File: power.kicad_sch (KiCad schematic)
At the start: 36 parts, among them J1 XT30PW-M, U1 ZXCT1107, U2 ST715M25R

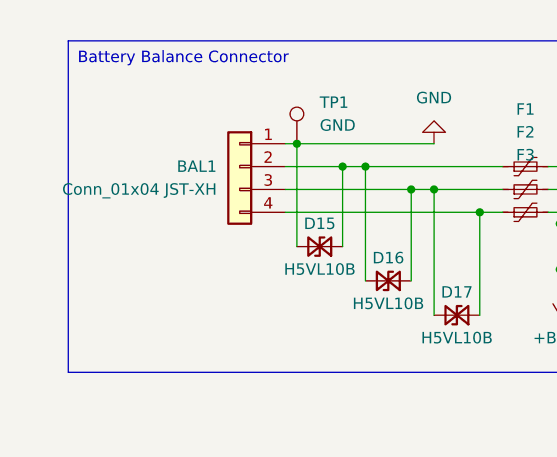
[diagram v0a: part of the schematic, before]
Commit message: Basic charging code, stupid power connector was reversed
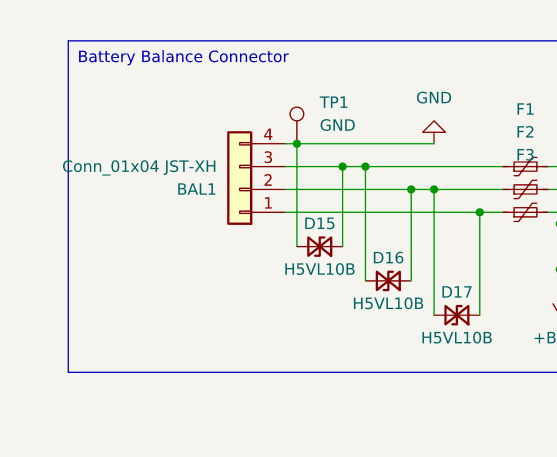
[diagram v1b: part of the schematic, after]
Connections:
- net GND: now also BAL1.4 (Pin_4); no longer BAL1.1 (Pin_1)
- net at D17.1 (A1), F3.1: now also BAL1.1 (Pin_1); no longer BAL1.4 (Pin_4)
- net at D15.1 (A1), D16.2 (A2), F1.1: now also BAL1.3 (Pin_3); no longer BAL1.2 (Pin_2)
- net at D16.1 (A1), D17.2 (A2), F2.1: now also BAL1.2 (Pin_2); no longer BAL1.3 (Pin_3)
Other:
- moved on the sheet: BAL1
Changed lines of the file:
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@@
 	(symbol
 		(lib_id "Connector_Generic:Conn_01x04")
-		(at 44.45 41.91 0)
-		(mirror y)
+		(at 44.45 44.45 180)
 		(unit 1)
 		(exclude_from_sim no)
@@
 		(dnp no)
 		(property "Reference" "BAL1"
-			(at 41.91 41.9099 0)
+			(at 41.91 44.4501 0)
 			(effects
 				(font
@@
 		)
 		(property "Value" "Conn_01x04 JST-XH"
-			(at 41.91 44.4499 0)
+			(at 41.91 41.9101 0)
 			(effects
 				(font
@@
 		)
 		(property "Footprint" "JakeLib:JST_XH_S4B-XH-A_1x04_P2.50mm_Horizontal_Tight"
-			(at 44.45 41.91 0)
+			(at 44.45 44.45 0)
 			(effects
 				(font
@@
 		)
 		(property "Datasheet" "~"
-			(at 44.45 41.91 0)
+			(at 44.45 44.45 0)
 			(effects
 				(font
@@
 		)
 		(property "Description" "Generic connector, single row, 01x04, script generated (kicad-library-utils/schlib/autogen/connector/)"
-			(at 44.45 41.91 0)
+			(at 44.45 44.45 0)
 			(effects
 				(font
@@
 		)
 		(property "LCSC_Code" "C157925"
-			(at 44.45 41.91 0)
+			(at 44.45 44.45 0)
 			(effects
 				(font

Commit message: Taking notes, doing some final adjustments to RC filter values
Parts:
- removed C6: .1u, Capacitor_SMD:C_0603_1608Metric, symbol Device:C
- removed D2: BAT54SW, Package_TO_SOT_SMD:SOT-323_SC-70, symbol Diode:BAT54SW
- removed R10, R11, R6, R7: 47.5k, Resistor_SMD:R_0402_1005Metric, symbol Device:R
- removed R8, R9: 220k, Resistor_SMD:R_0402_1005Metric, symbol Device:R
- added C17: .1u, Capacitor_SMD:C_0603_1608Metric, symbol Device:C
- added R31, R32: 150, Resistor_SMD:R_0402_1005Metric, symbol Device:R
- R4: value 220k -> 2k; footprint Resistor_SMD:R_0402_1005Metric -> Resistor_SMD:R_0603_1608Metric; LCSC_Code C851925 -> (none); Tolerance 0.5% -> (none)
- R5: value 220k -> 18k; footprint Resistor_SMD:R_0402_1005Metric -> Resistor_SMD:R_0603_1608Metric; LCSC_Code C851925 -> (none); Tolerance 0.5% -> (none)
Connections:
- net GND: now also R4.1, C17.1
- net SOLAR_CURRENT_ADC: now also C17.2, R32.2; no longer R1.1, U1.3 (OUT)
- net VSOLAR: now also R5.2
- net VSOLAR_ADC: now also R4.2, R5.1
- new net: R1.1, R31.1, U1.3 (OUT)
- new net: R31.2, R32.1
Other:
- note added: "25V*(2000/(20000))=2.5V 25V/20000ohms = 1.25mA current draw ~30mW power dissipation 1.8kohm Thevenin impedance"
- note added: "Measure current "before" the vsolar capacitor bank so you see the smoother average power draw"
- note added: "RC filter with TC ~5khz 16x attentuation @ 80khz pwm loop Only 300 ohm extra impedance for adc"
- note added: "Rsense = .1 ohm, @ 2 amps = 0.2V (Recommended for full range is 0.5V drop, but that's wasteful) Iout = 0.004 * Vsense so 3000 * .004*.2 = 2.4V @ 2 amps current"
- note added: "Solar input maxes: 50V capacitors 30V MOSFET Drain-Source Breakdown 30V TVS Diode"
- note added: "The ZXCT has a defined current that it outputs for a given voltage. This is fine if you never sample the signal. But I am seeing on the scope two spike with each PWM cycle. I think what's happening is that the ADC turns on, and there is all of a sudden a small 1000ohm path to ground while charging/discharging the ADC capacitor so probably to eliminate that you need an opamp"
- note removed: "Rsense = .1 ohm, @ 2 amps = 0.2V (Recommended for full range is 0.5V drop, but that's too much) Iout = 0.004 * Vsense so 3000 * .004*.2 = 2.4V @ 2 amps current"
- note removed: "Solar input maxes: 50V capacitors 30V MOSFET Drain-Source Breakdown 25V IRS2003 10V battery -> 20V charge pump, 2.5V gate-source = 17Volts"
- note removed: "Using || higher precision resistors to reduce absolute error on balancing Also, each divider uses the same range (even the 1S and 2S ones), so that you have consistency. 110k || 23.75k => 19.5k impedance 19.5k ohm * 0.1u cap = 2ms 12*(47.5/(47.5+220)) ~= 2.1V"
- moved on the sheet: C7, D1, D3, R1, TP3

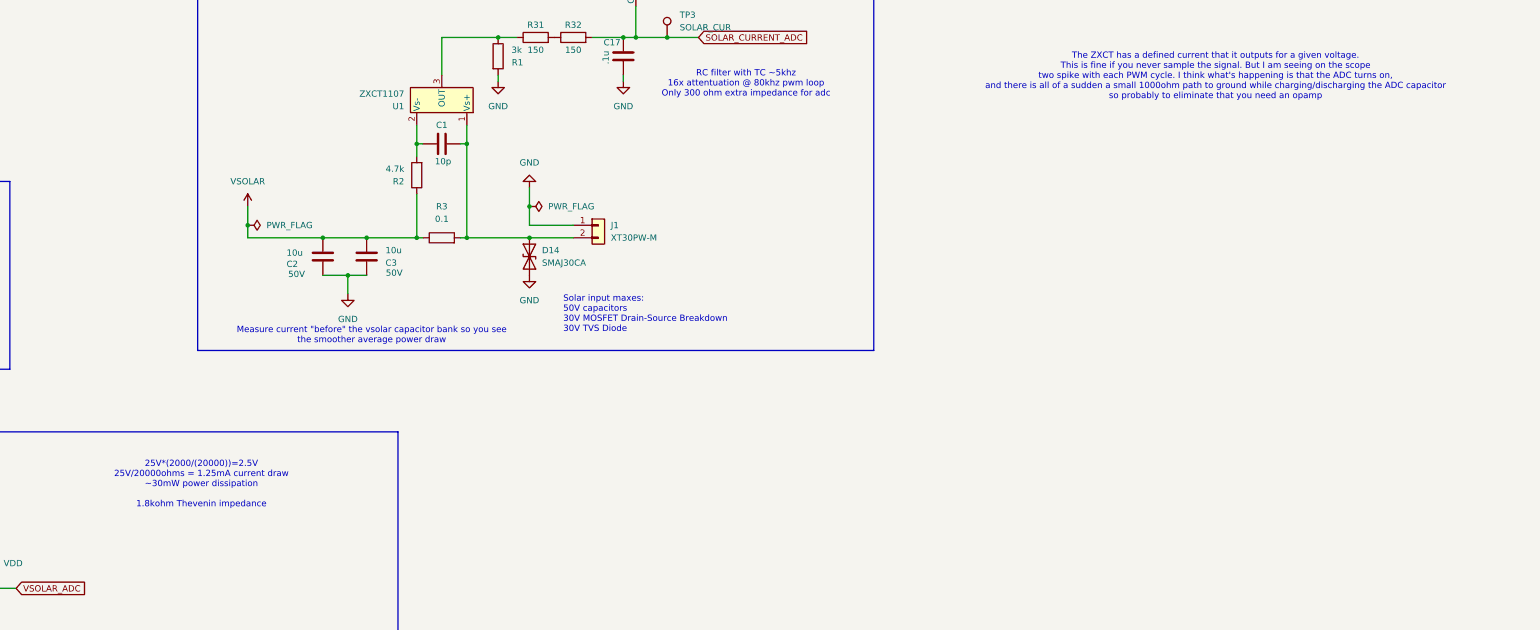
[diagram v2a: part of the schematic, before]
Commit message: L6388E mosfet drivers
Allow to enable/disable drivers
voltage dividers picked out
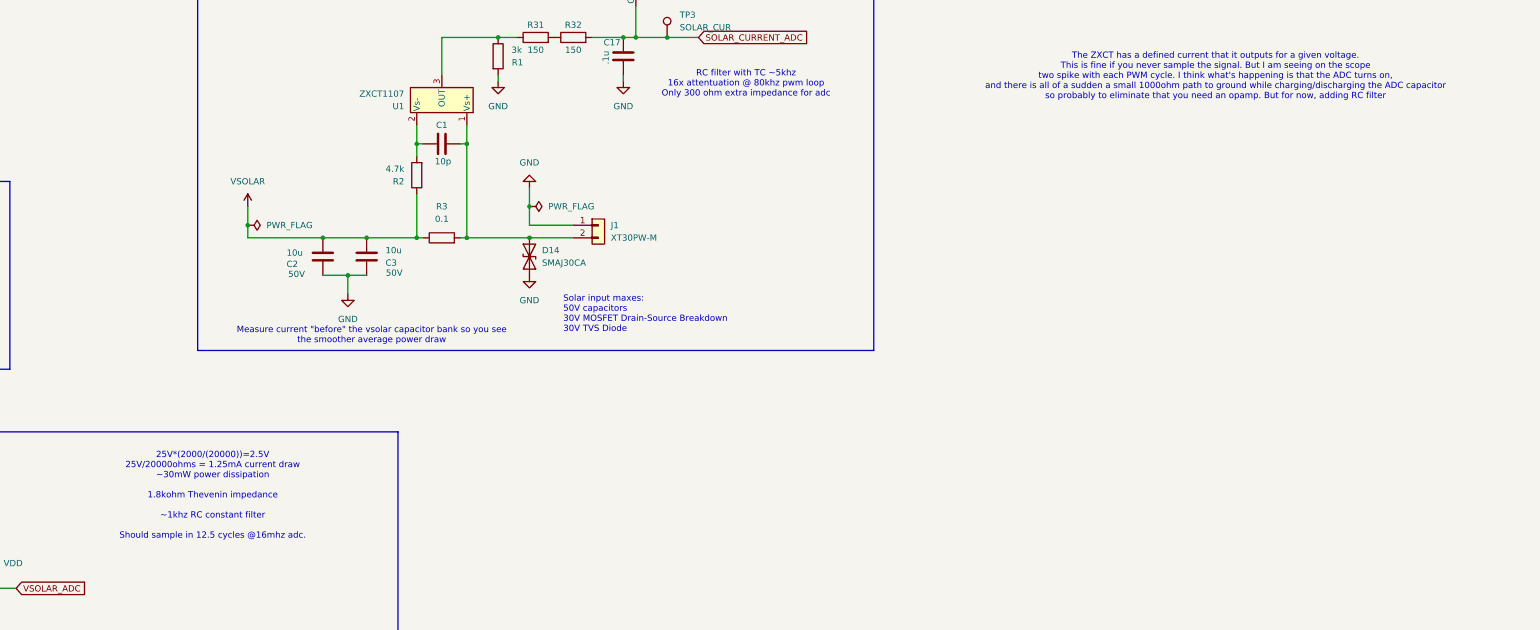
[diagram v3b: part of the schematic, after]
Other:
- note added: "25V*(2000/(20000))=2.5V 25V/20000ohms = 1.25mA current draw ~30mW power dissipation 1.8kohm Thevenin impedance ~1khz RC constant filter Should sample in 12.5 cycles @16mhz adc."
- note added: "The ZXCT has a defined current that it outputs for a given voltage. This is fine if you never sample the signal. But I am seeing on the scope two spike with each PWM cycle. I think what's happening is that the ADC turns on, and there is all of a sudden a small 1000ohm path to ground while charging/discharging the ADC capacitor so probably to eliminate that you need an opamp. But for now, adding R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"
- note removed: "25V*(2000/(20000))=2.5V 25V/20000ohms = 1.25mA current draw ~30mW power dissipation 1.8kohm Thevenin impedance"
- note removed: "The ZXCT has a defined current that it outputs for a given voltage. This is fine if you never sample the signal. But I am seeing on the scope two spike with each PWM cycle. I think what's happening is that the ADC turns on, and there is all of a sudden a small 1000ohm path to ground while charging/discharging the ADC capacitor so probably to eliminate that you need an opamp"
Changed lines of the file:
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@@
 		)
 	)
-	(text "The ZXCT has a defined current that it outputs for a given voltage.\nThis is fine if you never sample the signal. But I am seeing on the scope\ntwo spike with each PWM cycle. I think what's happening is that the ADC turns on,\nand there is all of a sudden a small 1000ohm path to ground while charging/discharging the ADC capacitor\nso probably to eliminate that you need an opamp"
+	(text "The ZXCT has a defined current that it outputs for a given voltage.\nThis is fine if you never sample the signal. But I am seeing on the scope\ntwo spike with each PWM cycle. I think what's happening is that the ADC turns on,\nand there is all of a sudden a small 1000ohm path to ground while charging/discharging the ADC capacitor\nso probably to eliminate that you need an opamp. But for now, adding RC filter"
 		(exclude_from_sim no)
 		(at 341.122 53.594 0)
@@
 		)
 	)
-	(text "25V*(2000/(20000))=2.5V\n25V/20000ohms = 1.25mA current draw\n~30mW power dissipation\n\n1.8kohm Thevenin impedance"
+	(text "25V*(2000/(20000))=2.5V\n25V/20000ohms = 1.25mA current draw\n~30mW power dissipation\n\n1.8kohm Thevenin impedance\n\n~1khz RC constant filter\n\nShould sample in 12.5 cycles @16mhz adc."
 		(exclude_from_sim no)
-		(at 135.382 136.398 0)
+		(at 137.668 138.684 0)
 		(effects
 			(font

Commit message: A couple of part selections
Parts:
- J1: LCSC_Code (none) -> C431092
- R4: LCSC_Code (none) -> C22975
- R5: LCSC_Code (none) -> C25810
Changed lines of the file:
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@@
 	(text "Solar input maxes:\n50V capacitors\n30V MOSFET Drain-Source Breakdown\n30V TVS Diode\n"
 		(exclude_from_sim no)
-		(at 208.788 101.854 0)
+		(at 229.108 100.33 0)
 		(effects
 			(font
@@
 			)
 		)
+		(property "LCSC_Code" "C22975"
+			(at 60.96 161.29 0)
+			(effects
+				(font
+					(size 1.27 1.27)
+				)
+				(hide yes)
+			)
+		)
 		(pin "2"
 		)
@@
 			)
 		)
+		(property "LCSC_Code" "C25810"
+			(at 53.34 157.48 0)
+			(effects
+				(font
+					(size 1.27 1.27)
+				)
+				(hide yes)
+			)
+		)
 		(pin "2"
 		)
@@
 			(at 215.9 83.82 0)
 			(effects
+				(font
+					(size 1.27 1.27)
+				)
+				(hide yes)
+			)
+		)
+		(property "LCSC_Code" "C431092"
+			(at 215.9 83.82 0)
+			(effects

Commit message: Layout
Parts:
- removed TP3: SOLAR_CUR, TestPoint:TestPoint_Loop_D2.60mm_Drill1.6mm_Beaded, symbol Connector:TestPoint
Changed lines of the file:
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@@
 	)
 	(junction
-		(at 229.87 45.72)
-		(diameter 0)
-		(color 0 0 0 0)
-	)
-	(junction
 		(at 189.23 67.31)
 		(diameter 0)
@@
 	(wire
 		(pts
-			(xy 229.87 45.72) (xy 236.22 45.72)
+			(xy 223.52 45.72) (xy 236.22 45.72)
 		)
 		(stroke
@@
 	(wire
 		(pts
-			(xy 223.52 45.72) (xy 229.87 45.72)
-		)
-		(stroke
-			(width 0)
-			(type default)
-		)
-	)
-	(wire
-		(pts
 			(xy 144.78 80.01) (xy 144.78 83.82)
 		)
@@
 					(unit 1)
 				)
-			)
-		)
-	)
-	(symbol
-		(lib_id "Connector:TestPoint")
-		(at 229.87 45.72 0)
-		(unit 1)
-		(exclude_from_sim no)
-		(in_bom yes)
-		(on_board yes)
-		(dnp no)
-		(fields_autoplaced yes)
-		(property "Reference" "TP3"
-			(at 232.41 41.1479 0)
-			(effects
-				(font
-					(size 1.27 1.27)
-				)
-				(justify left)
-			)
-		)
-		(property "Value" "SOLAR_CUR"
-			(at 232.41 43.6879 0)
-			(effects
-				(font
-					(size 1.27 1.27)
-				)
-				(justify left)
-			)
-		)
-		(property "Footprint" "TestPoint:TestPoint_Loop_D2.60mm_Drill1.6mm_Beaded"
-			(at 234.95 45.72 0)
-			(effects
-				(font
-					(size 1.27 1.27)
-				)
-				(hide yes)
-			)
-		)
-		(property "Datasheet" "~"
-			(at 234.95 45.72 0)
-			(effects
-				(font
-					(size 1.27 1.27)
-				)
-				(hide yes)
-			)
-		)
-		(property "Description" "test point"
-			(at 229.87 45.72 0)
-			(effects
-				(font
-					(size 1.27 1.27)
-				)
-				(hide yes)
-			)
-		)
-		(property "Sim.Device" ""
-			(at 229.87 45.72 0)
-			(effects
-				(font
-					(size 1.27 1.27)
-				)
-				(hide yes)
-			)
-		)
-		(property "Sim.Pins" ""
-			(at 229.87 45.72 0)
-			(effects
-				(font
-					(size 1.27 1.27)
-				)
-				(hide yes)
-			)
-		)
-		(property "Tolerance" ""
-			(at 229.87 45.72 0)
-			(effects
-				(font
-					(size 1.27 1.27)
-				)
-				(hide yes)
-			)
-		)
-		(pin "1"
-		)
-		(instances
-			(project "JPBms2"
-				(path "/d86e471c-a8be-422d-a5d1-5a4699b7b766/fda7e15b-dad1-4f54-abdb-4d4569bf33a6"
-					(reference "TP3")
-					(unit 1)
-				)

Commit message: Decent pass
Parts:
- removed TP4: VDD, TestPoint:TestPoint_Loop_D2.60mm_Drill1.6mm_Beaded, symbol Connector:TestPoint
- renumbered C4 to C1, C5 to C2, C7 to C3, C2 to C4, C3 to C5, C1 to C6, C17 to C7, D15 to D1, D16 to D2, D17 to D3, D3 to D4, D14 to D5, D1 to D6, R5 to R1, R4 to R2, R2 to R3, R3 to R4, R1 to R5, R31 to R6, R32 to R7, U2 to U1, U1 to U2
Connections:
- net Vs+: now reaches C6.1, D5.2 (A2), J1.2 (Pin_2), R4.2, U2.1 (Vs+)

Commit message: Routing pt1
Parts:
- renumbered C6 to C1, C7 to C17, C4 to C2, C5 to C3, C1 to C4, C2 to C5, C3 to C7, D6 to D1, D5 to D14, D1 to D15, D2 to D16, D3 to D17, D4 to D3, R5 to R1, R3 to R2, R4 to R3, R6 to R31, R7 to R32, R2 to R4, R1 to R5, U2 to U1, U1 to U2
